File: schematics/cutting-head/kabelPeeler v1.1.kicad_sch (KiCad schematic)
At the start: 62 parts, among them J1 Steppermotor, J2 Main input, J3 Limit switch, J4 Encoder, J5 LED-Output, J6 Ext Motor VCC, Q1 FDV301N, Q2 AO3401A, U1 XIAO-ESP32-S3-DIP, U2 TMC2209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

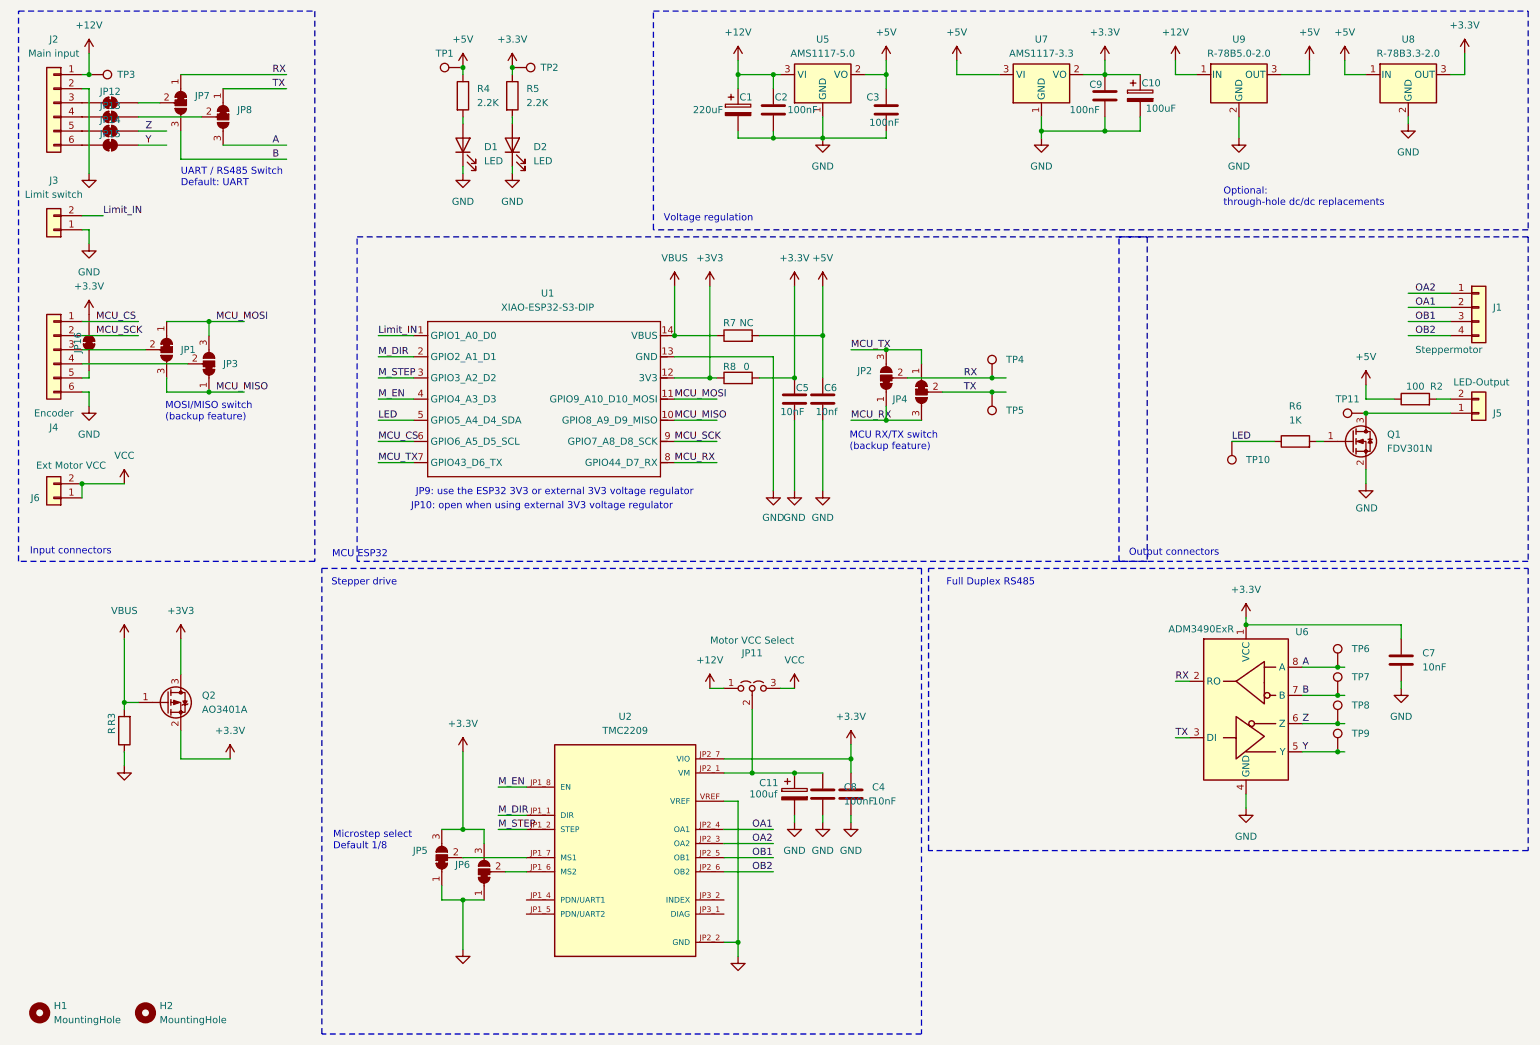
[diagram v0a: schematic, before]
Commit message: feat: cutting-head schematic v1.1
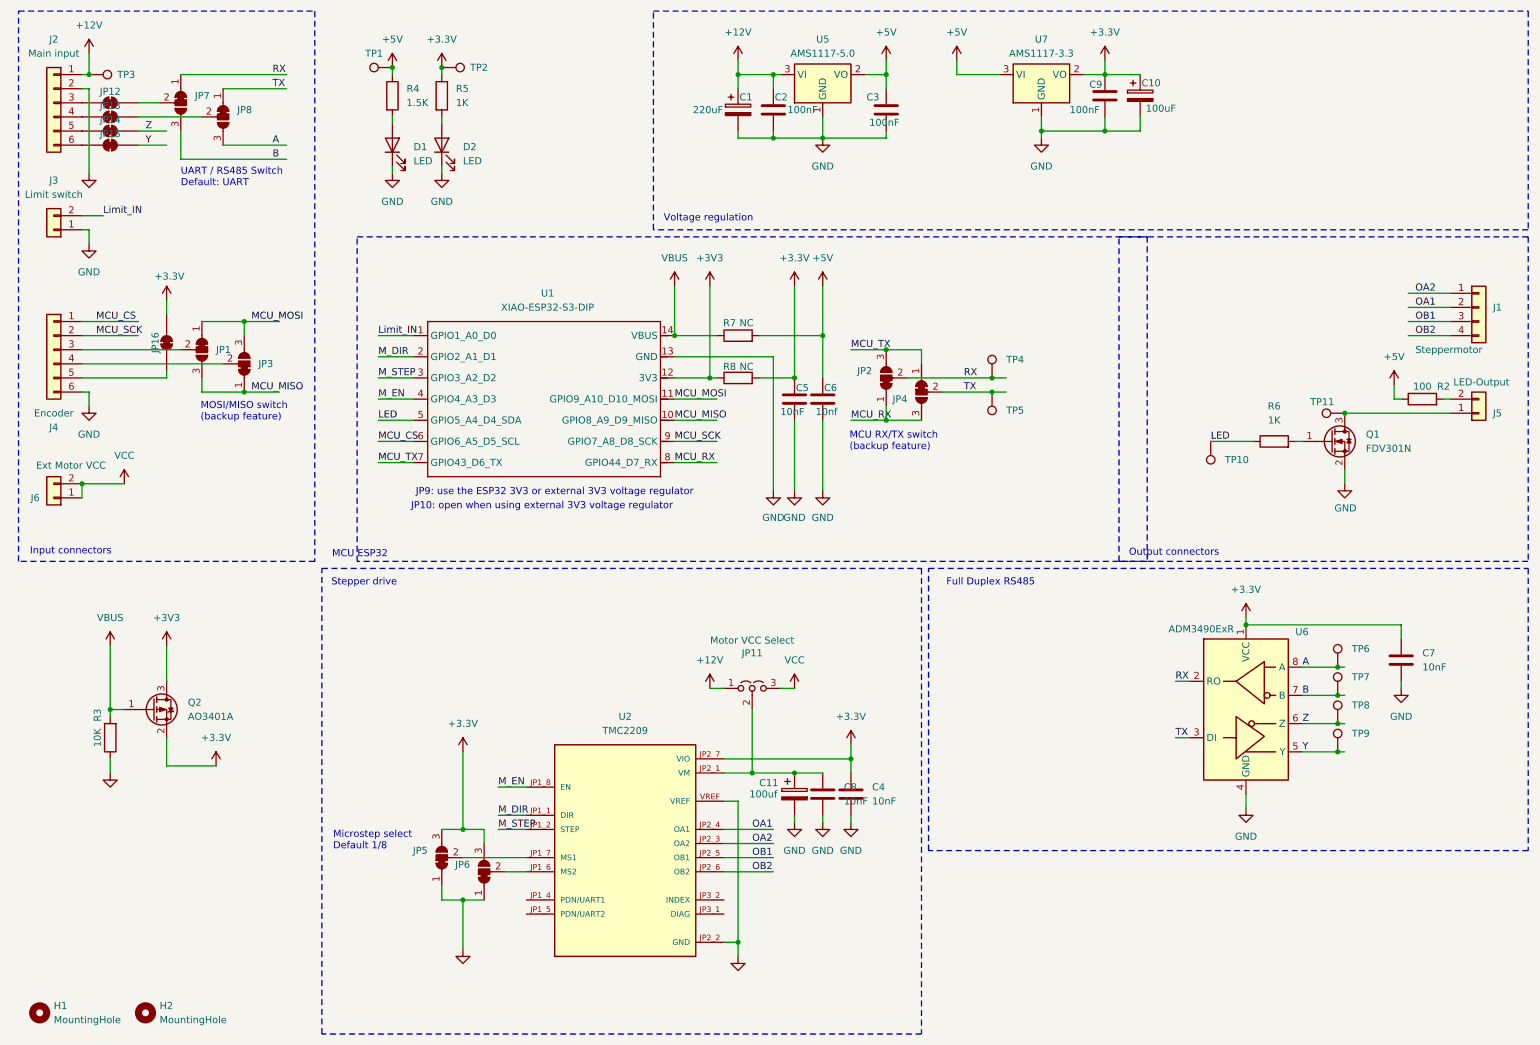
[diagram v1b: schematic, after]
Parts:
- removed U8: R-78B3.3-2.0, Converter_DCDC:Converter_DCDC_RECOM_R-78B-2.0_THT, symbol Converter_DCDC:R-78B3.3-2.0
- removed U9: R-78B5.0-2.0, Converter_DCDC:Converter_DCDC_RECOM_R-78B-2.0_THT, symbol Converter_DCDC:R-78B5.0-2.0
- C8: value 100nF -> 10nF
- R3: value R -> 10K
- R4: value 2.2K -> 1.5K
- R5: value 2.2K -> 1K
- R8: value 0 -> NC
- TP1, TP10, TP11, TP2, TP3, TP4, TP5, TP6, TP7, TP8, TP9: footprint TestPoint:TestPoint_Pad_D1.5mm -> TestPoint:TestPoint_Pad_D1.0mm
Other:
- note removed: "Optional: through-hole dc/dc replacements"
- moved on the sheet: D1, D2, JP1, JP16, JP3, Q1, R2, R4, R5, R6, TP1, TP10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
